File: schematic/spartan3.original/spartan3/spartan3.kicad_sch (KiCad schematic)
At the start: 287 parts, among them U1_clk_select_0 SPFT_Sliding_Switch-dynacore, U2 XC3S250E-4TQG144C

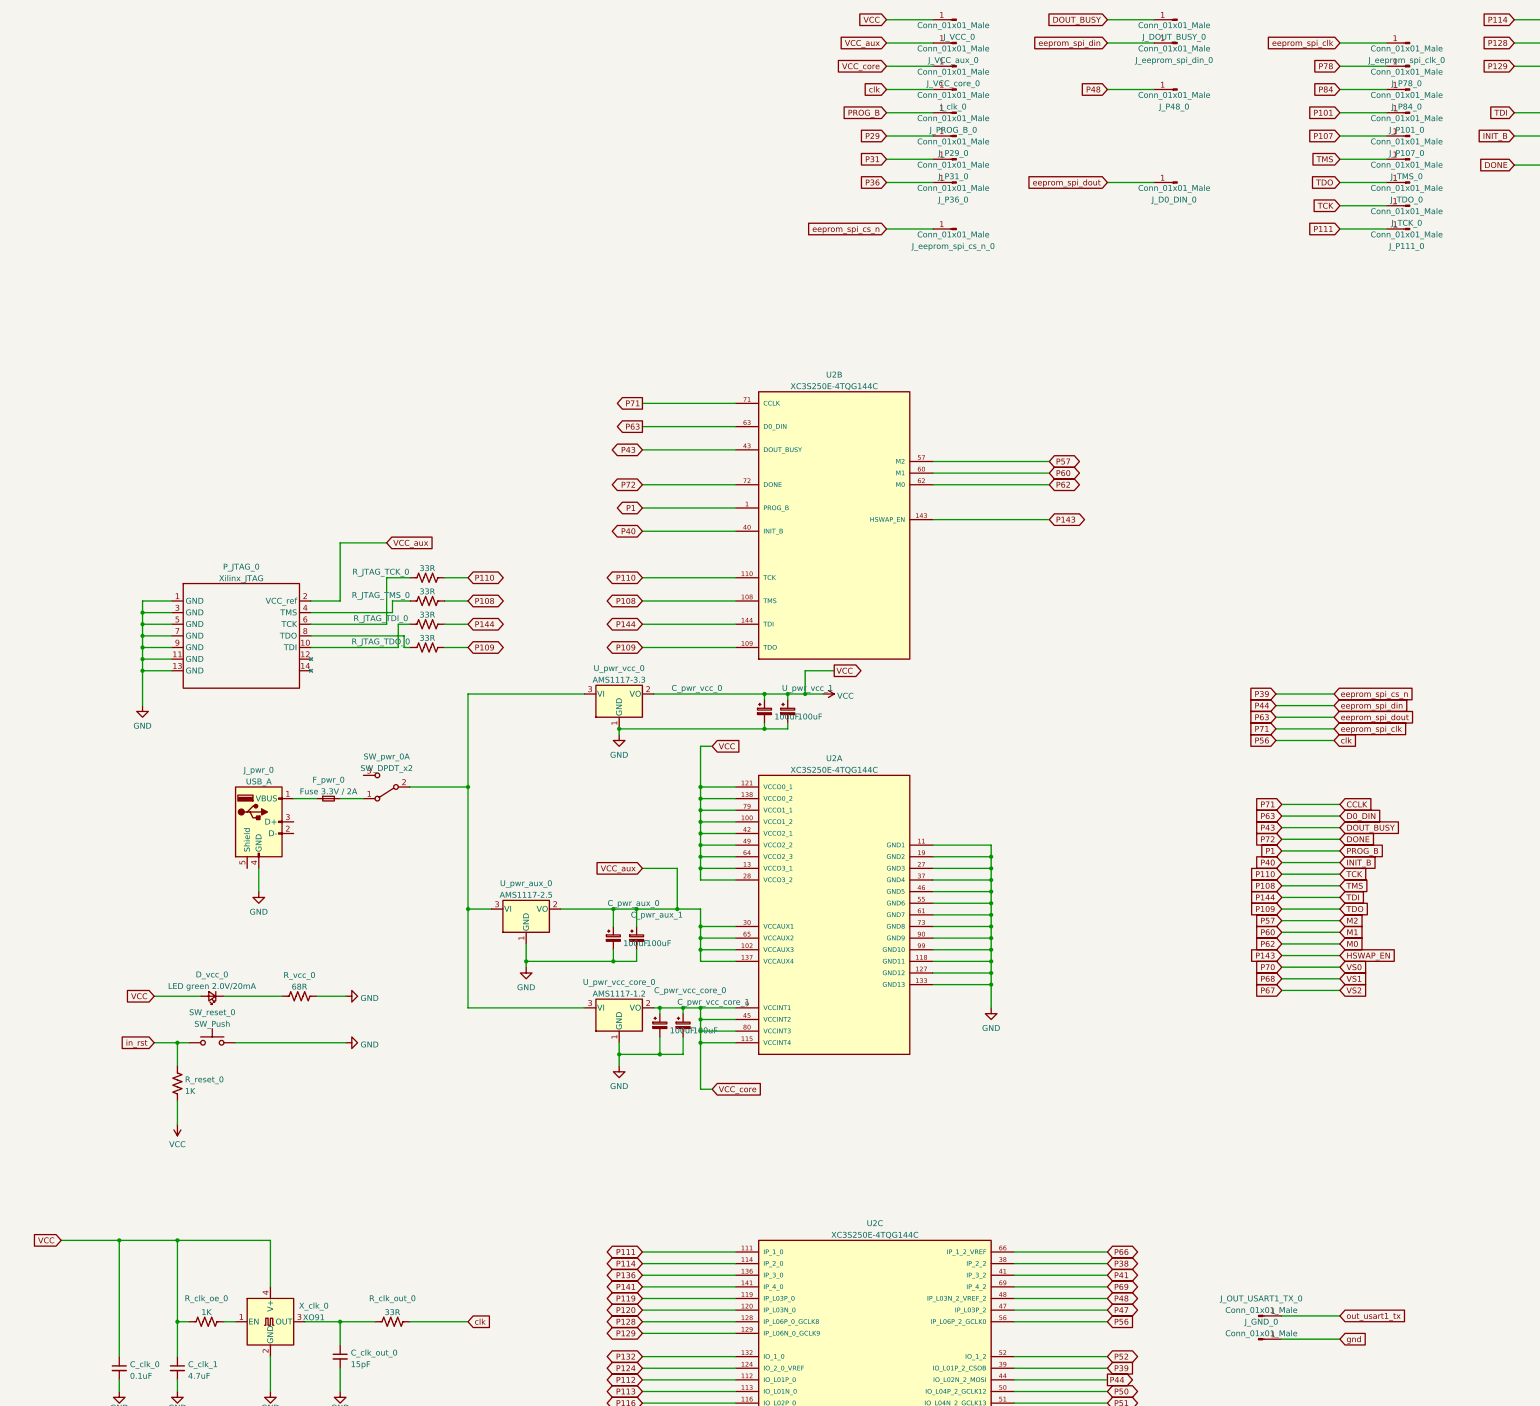
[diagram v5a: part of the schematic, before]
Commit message: Schematics/PCB layout updated. Gerber/Drill/BOM re-generated
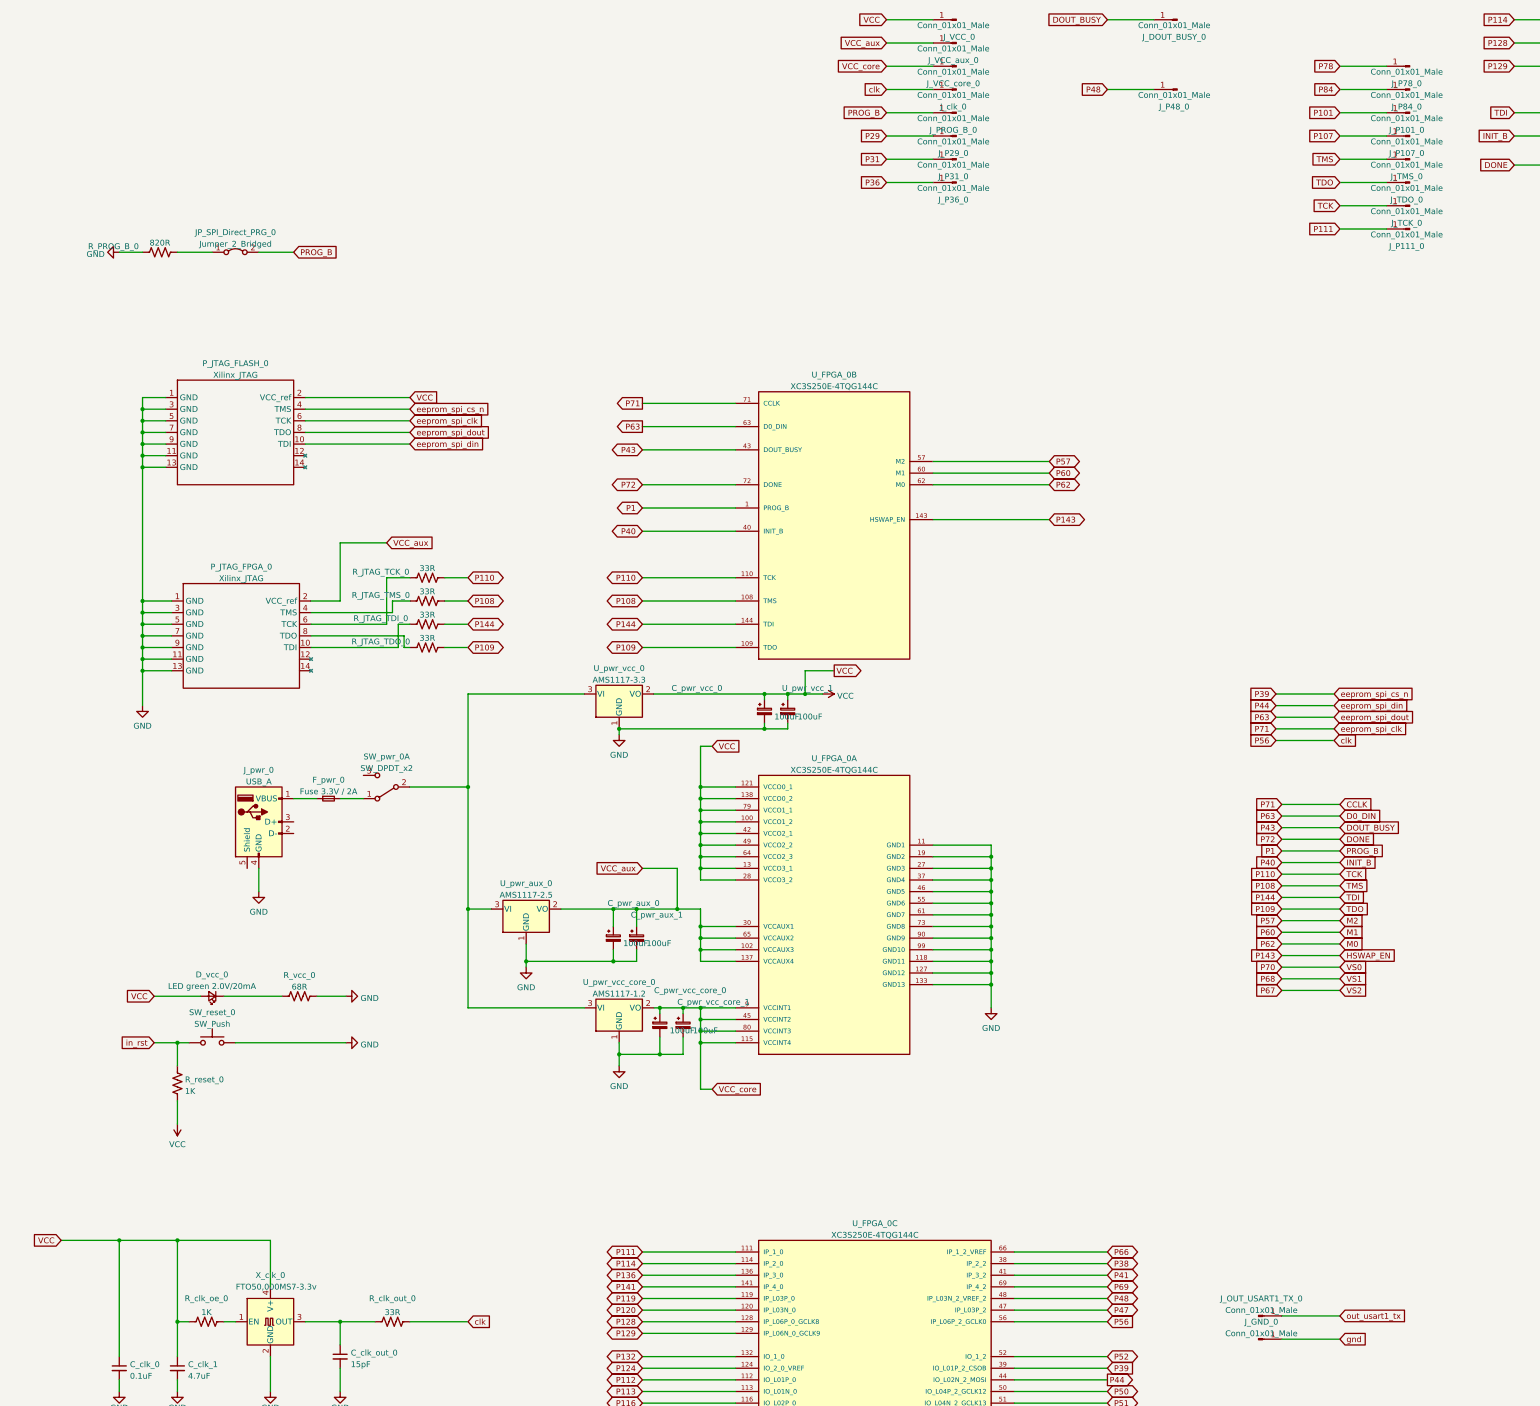
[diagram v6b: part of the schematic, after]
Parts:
- removed J_D0_DIN_0, J_eeprom_spi_clk_0, J_eeprom_spi_cs_n_0, J_eeprom_spi_din_0: Conn_01x01_Male, Connector_Wire:SolderWirePad_1x01_SMD_1x2mm, symbol Connector:Conn_01x01_Male
- added JP_SPI_Direct_PRG_0: Jumper_2_Bridged, Connector_PinHeader_2.54mm:PinHeader_1x02_P2.54mm_Vertical, symbol Jumper:Jumper_2_Bridged
- added P_JTAG_FLASH_0: Xilinx_JTAG, Connector_IDC:IDC-Header_2x07_P2.54mm_Vertical, symbol sliders:Xilinx_JTAG
- added R_PROG_B_0: 820R, Resistor_SMD:R_0805_2012Metric_Pad1.20x1.40mm_HandSolder, symbol Device:R_US
- P_JTAG_FPGA_0: renamed from P_JTAG_0; footprint Connector_IDC:IDC-Header_2x07-1MP_P2.54mm_Latch_Vertical -> Connector_IDC:IDC-Header_2x07_P2.54mm_Vertical
- X_clk_0: value XO91 -> FTO50,000MS7-3.3v
- renumbered U2 to U_FPGA_0
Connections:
- net CCLK: now also P_JTAG_FLASH_0.6 (TCK)
- net D0_DIN: now also P_JTAG_FLASH_0.8 (TDO)
- net GND: now also P_JTAG_FLASH_0.1 (GND), P_JTAG_FLASH_0.11 (GND), P_JTAG_FLASH_0.13 (GND), P_JTAG_FLASH_0.3 (GND), P_JTAG_FLASH_0.5 (GND), P_JTAG_FLASH_0.7 (GND), P_JTAG_FLASH_0.9 (GND), R_PROG_B_0.1
- net P1: now also JP_SPI_Direct_PRG_0.2 (B)
- net P39: now also P_JTAG_FLASH_0.4 (TMS)
- net P44: now also P_JTAG_FLASH_0.10 (TDI)
- net VCC: now also P_JTAG_FLASH_0.2 (VCC_ref)
- new net: JP_SPI_Direct_PRG_0.1 (A), R_PROG_B_0.2
